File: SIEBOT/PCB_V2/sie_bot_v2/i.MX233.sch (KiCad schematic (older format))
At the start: 87 parts, among them IC1 iMX233, J1 MICROSD, J2 POWER_5V, P1 CONN_12X2, P2 CONN_12X2, P3 CONN_1, P4 CONN_4X2, P5 CONN_1, P6 CONN_2, P7 CONN_1, Q1 MMDT3904, SW3 RESET, U1 ADM3101E, X1 24MHz

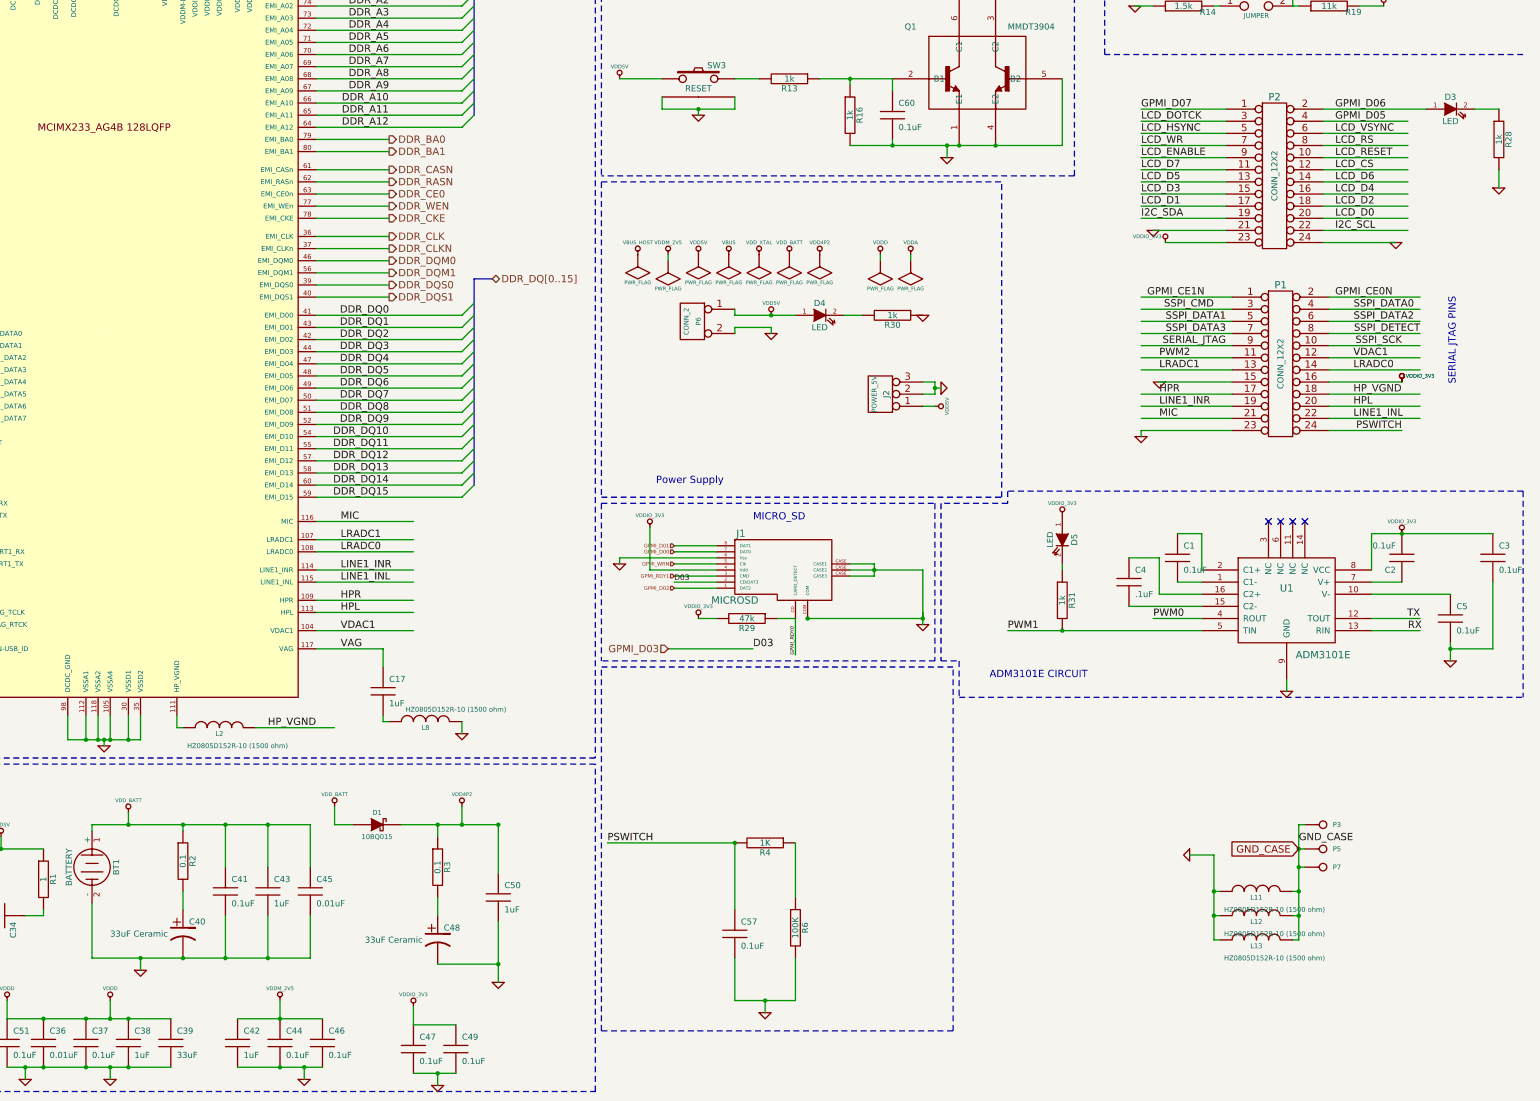
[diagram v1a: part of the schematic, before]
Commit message: Conexión del STM32 con el procesador, adición de un regulador de 3.3V disponible para el usuario
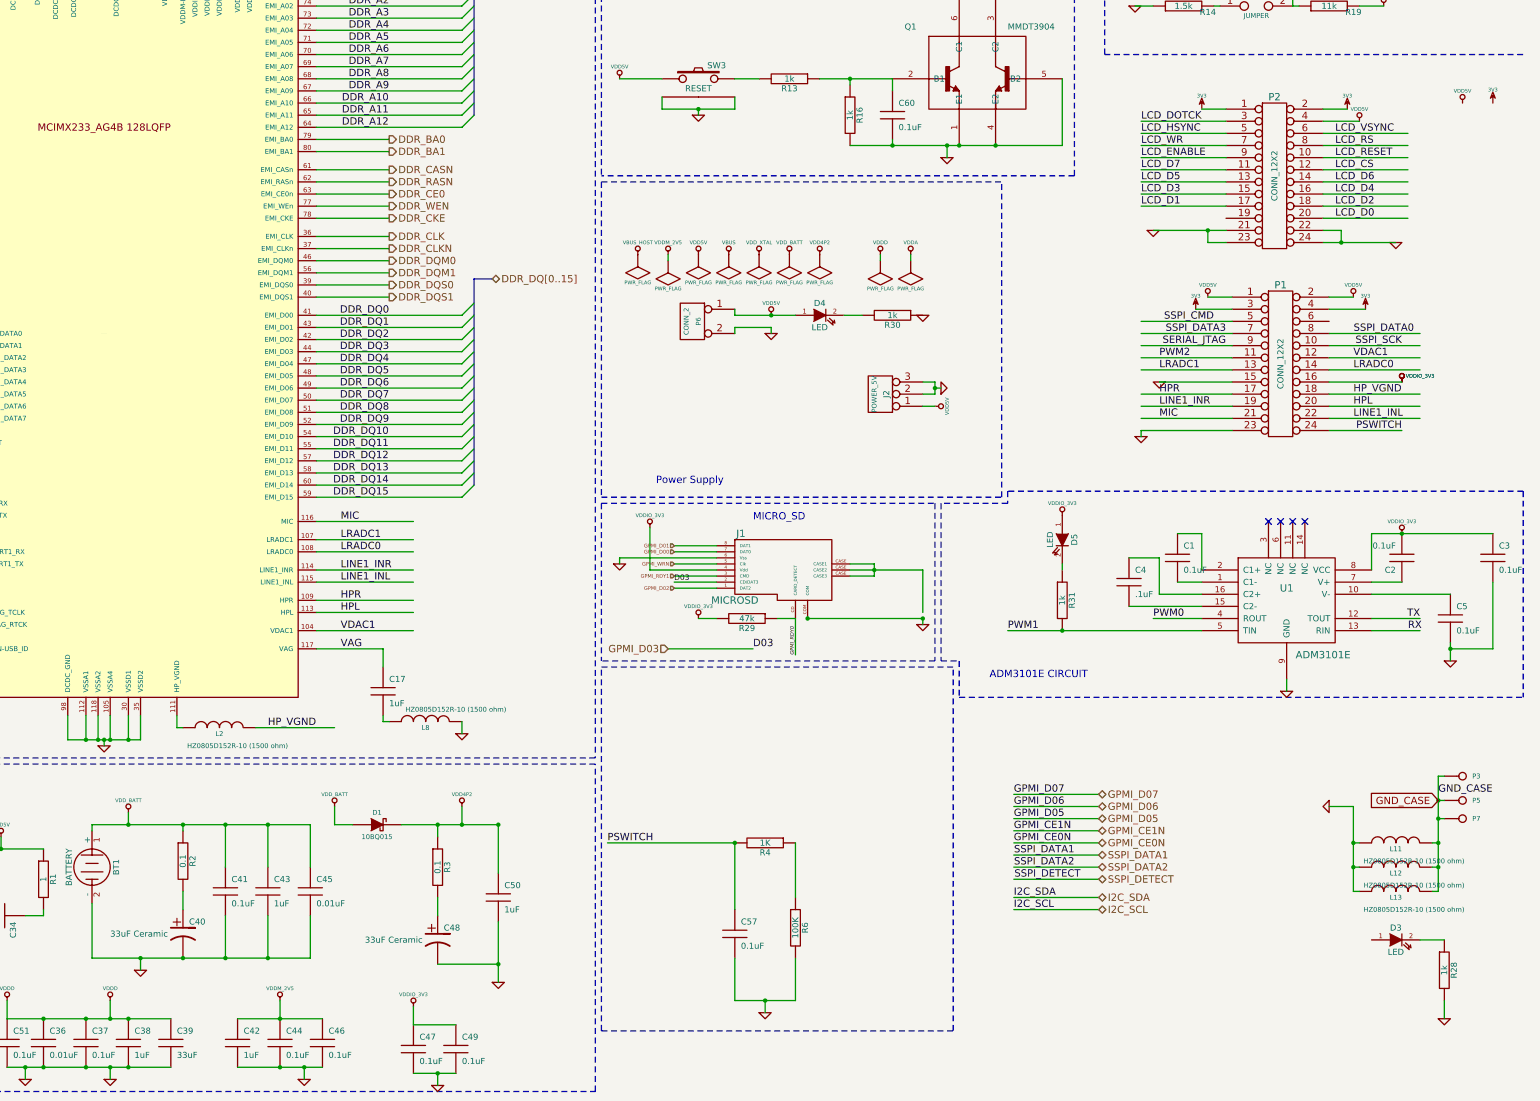
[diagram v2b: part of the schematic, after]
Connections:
- net labels added: 3V3
- wire segments 383 -> 393
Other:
- note removed: "SERIAL JTAG PINS"
- moved on the sheet: D3, L11, L12, L13, P3, P5, P7, R28

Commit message: Ruteo de la conexión entre el procesador y el STM32, re-localización de los conectores de alimentación y USB, adidición del regulador de 3.3V
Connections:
- net labels added: USB_M2, USM_P2
- net labels removed: GPMI_D03
- wire segments 393 -> 396

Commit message: Inicio de la conexión de los Puente H
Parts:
- added P10: CONN_1, MHOLE, symbol CONN_1
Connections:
- wire segments 396 -> 397
